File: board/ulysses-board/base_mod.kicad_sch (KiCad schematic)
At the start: 33 parts, among them J3 RS-232, J4 LC display, Q2 BC548, Q3 BC548, SW10 Config, SW3 UP, SW4 Ri, SW5 DN, SW6 Le, SW7 OK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

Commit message: Make some minor fixes.
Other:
- moved on the sheet: R19, SW10, SW3, SW4, SW5, SW6, SW7, SW8, SW9, U7

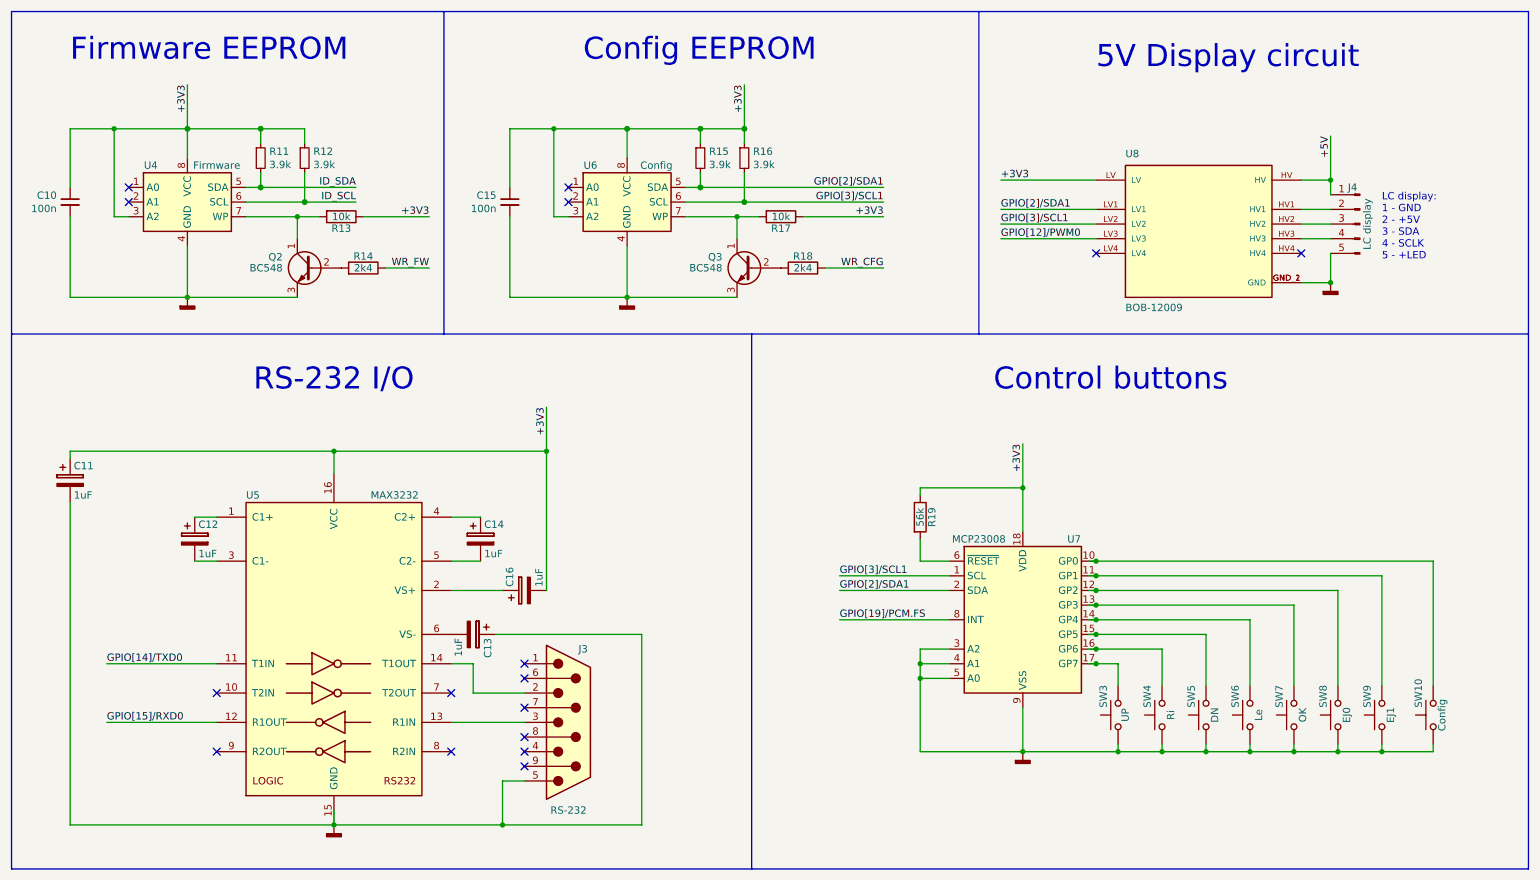
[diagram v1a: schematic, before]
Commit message: Add a real-time clock.
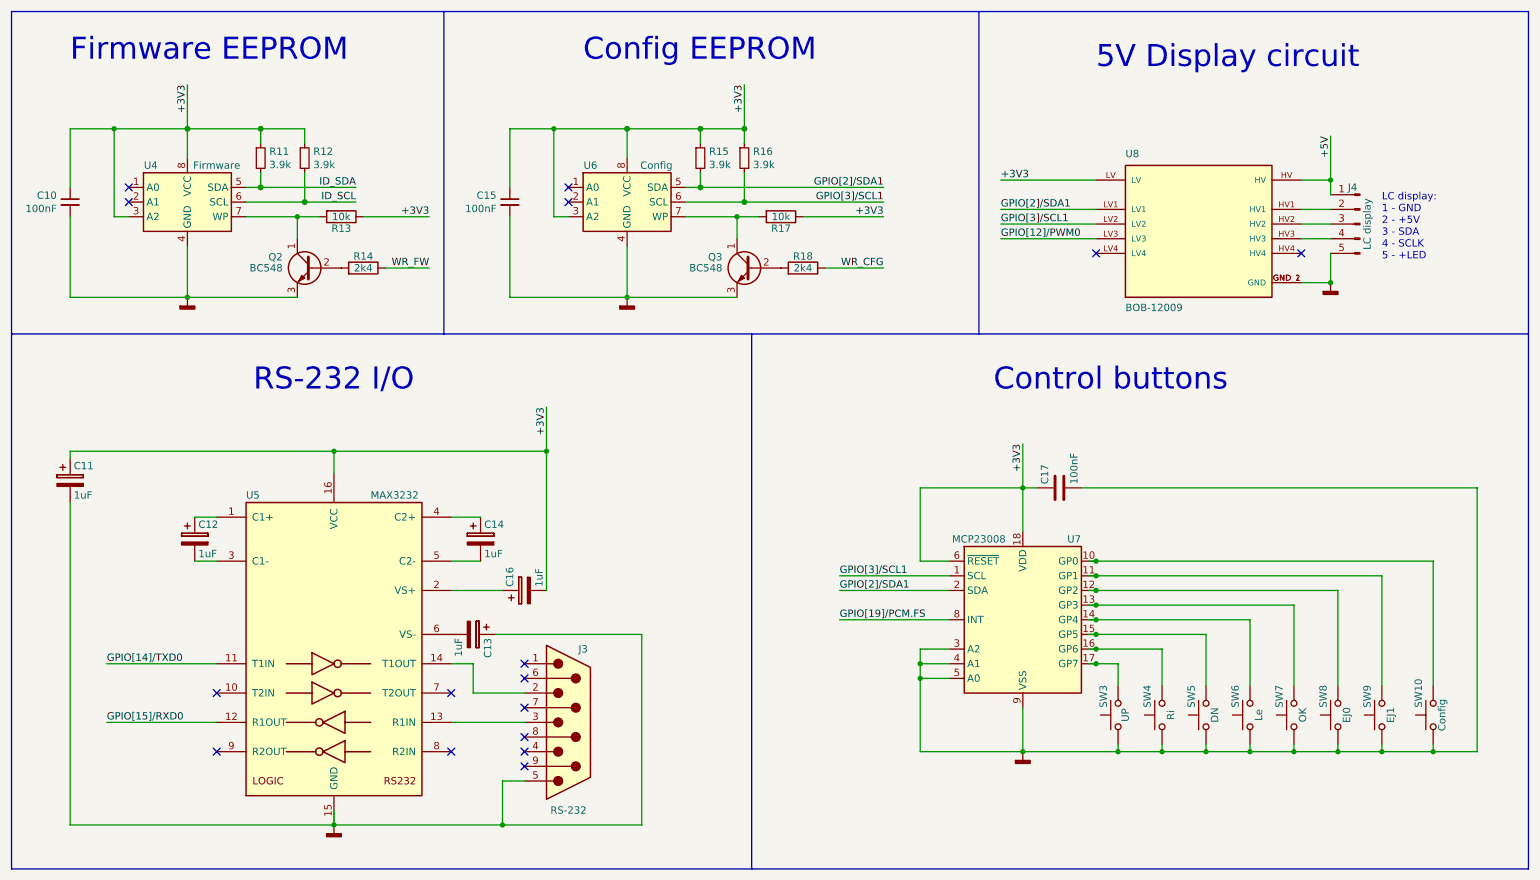
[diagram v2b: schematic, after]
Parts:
- removed R19: 56k, symbol Device:R
- added C17: 100nF, symbol Device:C
- C10, C15: value 100n -> 100nF
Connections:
- net +3V3: now also U7.6 (~{RESET}), C17.1
- net GNDD: now also C17.2
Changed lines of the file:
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@@
   (title_block
     (title "The Ulysses Board")
-    (date "2022-08-29")
+    (date "2022-09-01")
     (rev "1.2")
     (company "Dirk Gottschalk")
@@
   )
   (junction (at 44.45 62.23) (diameter 0) (color 0 0 0 0)
+  )
+  (junction (at 260.35 140.97) (diameter 0) (color 0 0 0 0)
   )
   (junction (at 228.6 140.97) (diameter 0) (color 0 0 0 0)
@@
     (stroke (width 0) (type default) (color 0 0 0 0))
   )
+  (wire (pts (xy 267.97 140.97) (xy 260.35 140.97))
+    (stroke (width 0) (type default) (color 0 0 0 0))
+  )
   (wire (pts (xy 69.85 92.71) (xy 69.85 88.9))
     (stroke (width 0) (type default) (color 0 0 0 0))
@@
     (stroke (width 0) (type solid) (color 0 0 0 0))
   )
-  (wire (pts (xy 171.45 95.25) (xy 171.45 96.52))
-    (stroke (width 0) (type default) (color 0 0 0 0))
-  )
   (wire (pts (xy 95.25 107.95) (xy 90.17 107.95))
     (stroke (width 0) (type default) (color 0 0 0 0))
@@
     (stroke (width 0) (type default) (color 0 0 0 0))
   )
+  (wire (pts (xy 189.23 95.25) (xy 191.77 95.25))
+    (stroke (width 0) (type default) (color 0 0 0 0))
+  )
   (wire (pts (xy 189.23 87.63) (xy 189.23 95.25))
     (stroke (width 0) (type default) (color 0 0 0 0))
@@
     (stroke (width 0) (type default) (color 0 0 0 0))
   )
-  (wire (pts (xy 171.45 104.14) (xy 171.45 107.95))
+  (wire (pts (xy 171.45 95.25) (xy 171.45 107.95))
     (stroke (width 0) (type default) (color 0 0 0 0))
   )
@@
     (stroke (width 0) (type default) (color 0 0 0 0))
   )
+  (wire (pts (xy 199.39 95.25) (xy 267.97 95.25))
+    (stroke (width 0) (type default) (color 0 0 0 0))
+  )
   (wire (pts (xy 93.98 130.81) (xy 93.98 125.73))
     (stroke (width 0) (type default) (color 0 0 0 0))
@@
   )
   (wire (pts (xy 110.49 48.26) (xy 107.95 48.26))
+    (stroke (width 0) (type default) (color 0 0 0 0))
+  )
+  (wire (pts (xy 267.97 95.25) (xy 267.97 140.97))
     (stroke (width 0) (type default) (color 0 0 0 0))
   )
@@
     (pin "2")
   )
+  (symbol (lib_id "Device:C") (at 195.58 95.25 90) (unit 1)
+    (in_bom yes) (on_board yes)
+    (property "Reference" "C17" (id 0) (at 193.04 94.615 0)
+      (effects (font (size 1.27 1.27)) (justify left))
+    )
+    (property "Value" "100nF" (id 1) (at 198.12 94.615 0)
+      (effects (font (size 1.27 1.27)) (justify left))
+    )
+    (property "Footprint" "" (id 2) (at 199.39 94.2848 0)
+      (effects (font (size 1.27 1.27)) hide)
+    )
+    (property "Datasheet" "~" (id 3) (at 195.58 95.25 0)
+      (effects (font (size 1.27 1.27)) hide)
+    )
+    (pin "1")
+    (pin "2")
+  )
   (symbol (lib_id "Device:C_Small") (at 100.33 45.72 0) (unit 1)
     (in_bom yes) (on_board yes)
@@
       (effects (font (size 1.27 1.27)) (justify right))
     )
-    (property "Value" "100n" (id 1) (at 98.0058 46.8693 0)
+    (property "Value" "100nF" (id 1) (at 98.0058 46.8693 0)
       (effects (font (size 1.27 1.27)) (justify right))
     )
@@
   (symbol (lib_id "power:GNDD") (at 44.45 62.23 0) (unit 1)
     (in_bom yes) (on_board yes)
-    (property "Reference" "#PWR05" (id 0) (at 44.45 68.58 0)
+    (property "Reference" "#PWR04" (id 0) (at 44.45 68.58 0)
       (effects (font (size 1.27 1.27)) hide)
     )
@@
   (symbol (lib_id "power:GNDD") (at 69.85 153.67 0) (unit 1)
     (in_bom yes) (on_board yes)
-    (property "Reference" "#PWR06" (id 0) (at 69.85 160.02 0)
+    (property "Reference" "#PWR05" (id 0) (at 69.85 160.02 0)
       (effects (font (size 1.27 1.27)) hide)
     )
@@
   (symbol (lib_id "power:GNDD") (at 189.23 140.97 0) (unit 1)
     (in_bom yes) (on_board yes)
-    (property "Reference" "#PWR010" (id 0) (at 189.23 147.32 0)
+    (property "Reference" "#PWR07" (id 0) (at 189.23 147.32 0)
       (effects (font (size 1.27 1.27)) hide)
     )
@@
   (symbol (lib_id "power:GNDD") (at 242.57 59.69 0) (unit 1)
     (in_bom yes) (on_board yes)
-    (property "Reference" "#PWR012" (id 0) (at 242.57 66.04 0)
+    (property "Reference" "#PWR08" (id 0) (at 242.57 66.04 0)
       (effects (font (size 1.27 1.27)) hide)
     )
@@
     )
     (pin "1")
-  )
-  (symbol (lib_id "Device:R") (at 171.45 100.33 0) (unit 1)
-    (in_bom yes) (on_board yes)
-    (property "Reference" "R19" (id 0) (at 173.482 100.33 90))
-    (property "Value" "56k" (id 1) (at 171.45 100.33 90))
-    (property "Footprint" "" (id 2) (at 169.672 100.33 90)
-      (effects (font (size 1.27 1.27)) hide)
-    )
-    (property "Datasheet" "~" (id 3) (at 171.45 100.33 0)
-      (effects (font (size 1.27 1.27)) hide)
-    )
-    (pin "1")
-    (pin "2")
   )
   (symbol (lib_id "Interface_Expansion:MCP23008-xP") (at 189.23 118.11 0) (unit 1)
@@
       (effects (font (size 1.27 1.27)) (justify right))
     )
-    (property "Value" "100n" (id 1) (at 21.8058 46.8693 0)
+    (property "Value" "100nF" (id 1) (at 21.8058 46.8693 0)
       (effects (font (size 1.27 1.27)) (justify right))
     )
@@
   (symbol (lib_id "power:GNDD") (at 120.65 62.23 0) (unit 1)
     (in_bom yes) (on_board yes)
-    (property "Reference" "#PWR08" (id 0) (at 120.65 68.58 0)
-      (effects (font (size 1.27 1.27)) hide)
-    )
+    (property "Reference" "#PWR06" (id 0) (at 120.65 68.58 0)
+      (effects (font (size 1.27 1.27)) hide)
+    )

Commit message: Make schemaics more readable.
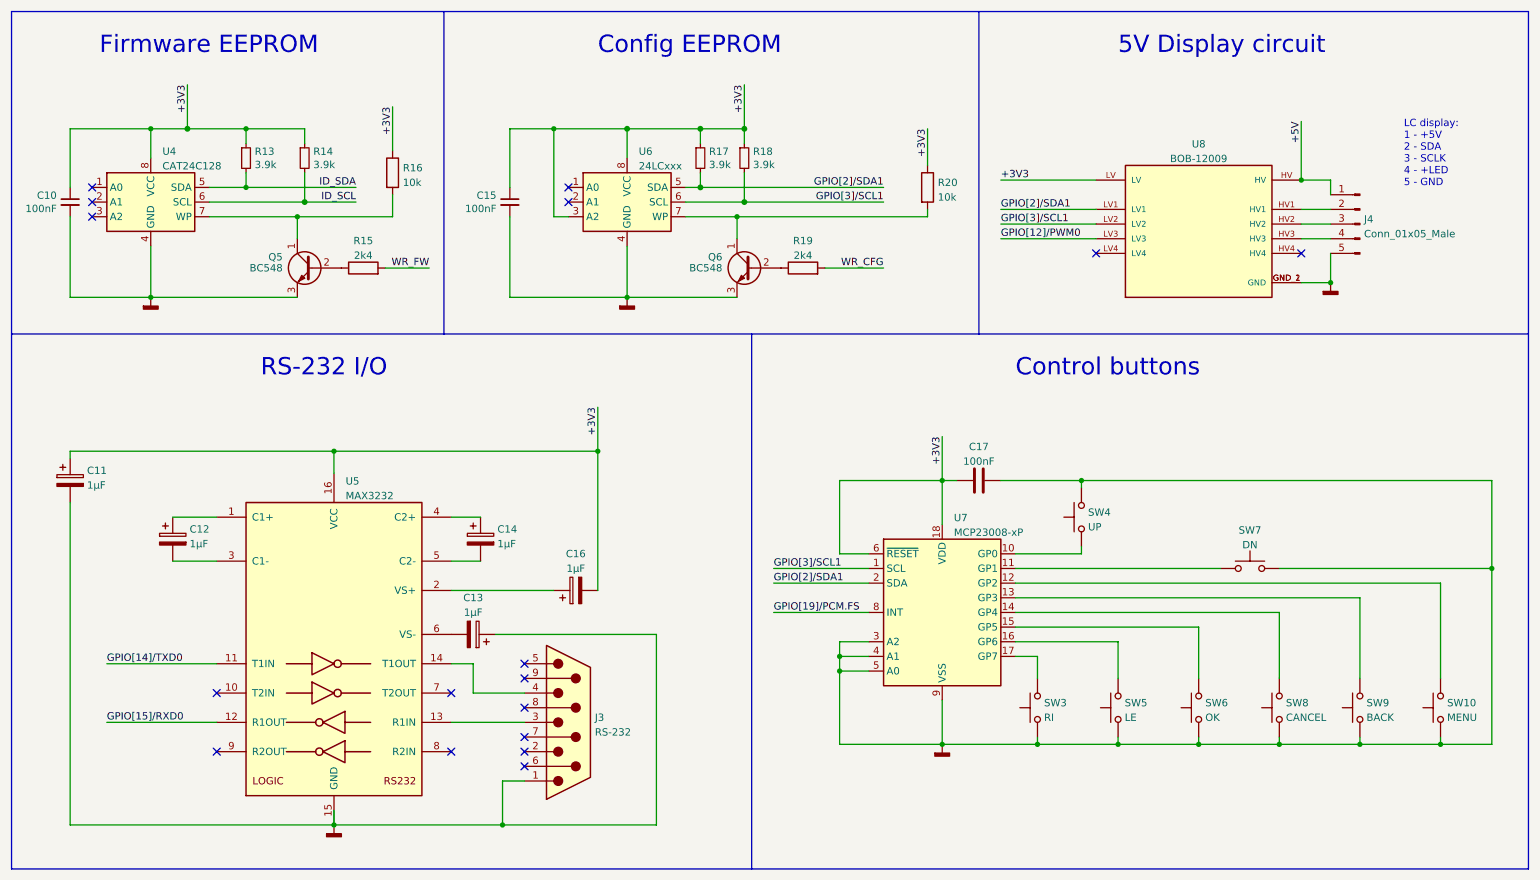
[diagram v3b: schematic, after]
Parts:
- removed C11: 1uF, Capacitor_THT:CP_Radial_D12.5mm_P2.50mm, symbol Pi-Board-rescue:CP
- removed C12, C13, C14: 1uF, Capacitors_THT:CP_Radial_D12.5mm_P5.00mm, symbol Pi-Board-rescue:CP
- removed C16: 1uF, symbol Pi-Board-rescue:CP
- removed R13, R17: 10k, symbol Device:R
- removed R14, R18: 2k4, symbol Device:R
- removed U4: Firmware, Package_DIP:DIP-8_W7.62mm_Socket_LongPads, symbol Memory_EEPROM:CAT24C256
- removed U6: Config, Package_DIP:DIP-8_W7.62mm_Socket_LongPads, symbol Memory_EEPROM:CAT24C256
- added C11, C12, C13, C14, C16: 1µF, symbol Device:C_Polarized
- added R15, R19: 2k4, symbol Device:R
- added R16, R20: 10k, symbol Device:R
- added U4: CAT24C128, Package_DIP:DIP-8_W7.62mm_LongPads, symbol Memory_EEPROM:CAT24C128
- added U6: 24LCxxx, symbol Memory_EEPROM:24LC1025
- J3: footprint Connector_Dsub:DSUB-9_Male_Horizontal_P2.77x2.84mm_EdgePinOffset9.40mm -> (none)
- J4: value LC display -> Conn_01x05_Male; footprint Connector_PinHeader_2.54mm:PinHeader_1x05_P2.54mm_Vertical -> (none)
- SW10: value Config -> MENU; footprint (none) -> Button_Switch_SMD:SW_MEC_5GSH9
- SW3: value UP -> RI; footprint (none) -> Button_Switch_SMD:SW_MEC_5GSH9
- SW4: value Ri -> UP
- SW5: value DN -> LE; footprint (none) -> Button_Switch_SMD:SW_MEC_5GSH9
- SW6: value Le -> OK; footprint (none) -> Button_Switch_SMD:SW_MEC_5GSH9
- SW7: value OK -> DN
- SW8: value EJ0 -> CANCEL; footprint (none) -> Button_Switch_SMD:SW_MEC_5GSH9
- SW9: value EJ1 -> BACK; footprint (none) -> Button_Switch_SMD:SW_MEC_5GSH9
- U5: footprint Package_DIP:DIP-14_W10.16mm -> (none)
- U7: value MCP23008 -> MCP23008-xP
- renumbered Q2 to Q5, Q3 to Q6, R11 to R13, R12 to R14, R15 to R17, R16 to R18
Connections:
- net +3V3: now also C11.1, C16.2, R16.1, R20.1, U4.8 (VCC), U6.3 (A2), U6.8 (VCC)
- net GNDD: now also J3.1, SW4.2, SW7.2, C11.2, C13.1, U4.4 (GND), U6.4 (GND); no longer J3.5, SW4.1, SW7.1
- net GPIO[2]/SDA1: now also U6.5 (SDA)
- net GPIO[3]/SCL1: now also U6.6 (SCL)
- net ID_SCL: now also U4.6 (SCL)
- net ID_SDA: now also U4.5 (SDA)
- net WR_CFG: now also R19.2
- net WR_FW: now also R15.2
- net at U7.16 (GP6): now also SW5.2; no longer SW4.2
- net at U5.1 (C1+): now also C12.1
- net at U5.3 (C1-): now also C12.2
- net at Q6.2 (B): now also R19.1
- net at Q5.1 (C): now also R16.2, U4.7 (WP)
- net at Q5.2 (B): now also R15.1
- net at J3.2: no longer U5.14 (T1OUT)
- net at J3.4: now also U5.14 (T1OUT)
- net at U7.12 (GP2): now also SW10.2; no longer SW8.2
- net at U7.10 (GP0): now also SW4.1; no longer SW10.2
- net at U5.4 (C2+): now also C14.1
- net at U5.5 (C2-): now also C14.2
- net at U7.15 (GP5): now also SW6.2; no longer SW5.2
- net at Q6.1 (C): now also R20.2, U6.7 (WP)
- net at U7.11 (GP1): now also SW7.1; no longer SW9.2
- net at U7.13 (GP3): now also SW9.2; no longer SW7.2
- net at U7.14 (GP4): now also SW8.2; no longer SW6.2
- net at U5.2 (VS+): now also C16.1
- net at U5.6 (VS-): now also C13.2
- no-connect marks 16 -> 17
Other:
- note added: "LC display: 1 - +5V 2 - SDA 3 - SCLK 4 - +LED 5 - GND"
- note removed: "LC display: 1 - GND 2 - +5V 3 - SDA 4 - SCLK 5 - +LED"
- moved on the sheet: R13

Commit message: Some minor imptovements.
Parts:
- J4: value Conn_01x05_Male -> LCD
- U4: value CAT24C128 -> AT24C1024B
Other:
- moved on the sheet: J4, U8
